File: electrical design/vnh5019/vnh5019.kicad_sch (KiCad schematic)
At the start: 20 parts, among them J1 XT30UPBF, J2 SH 1.0 6P, J3 Conn_01x01_Female, J4 Conn_01x01_Female, Q1 Q_NMOS_GDS, U1 VNH5019A-E

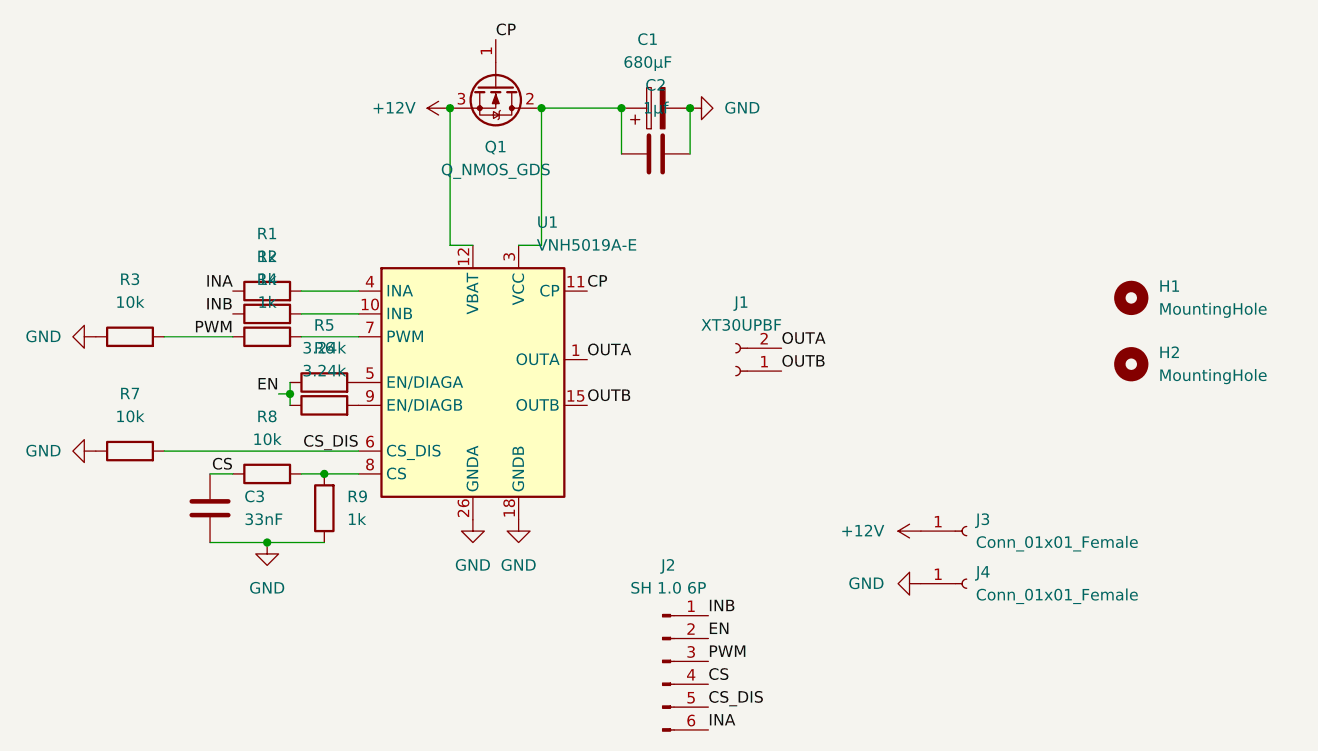
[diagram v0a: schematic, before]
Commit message: change driver output connector to 5 pins
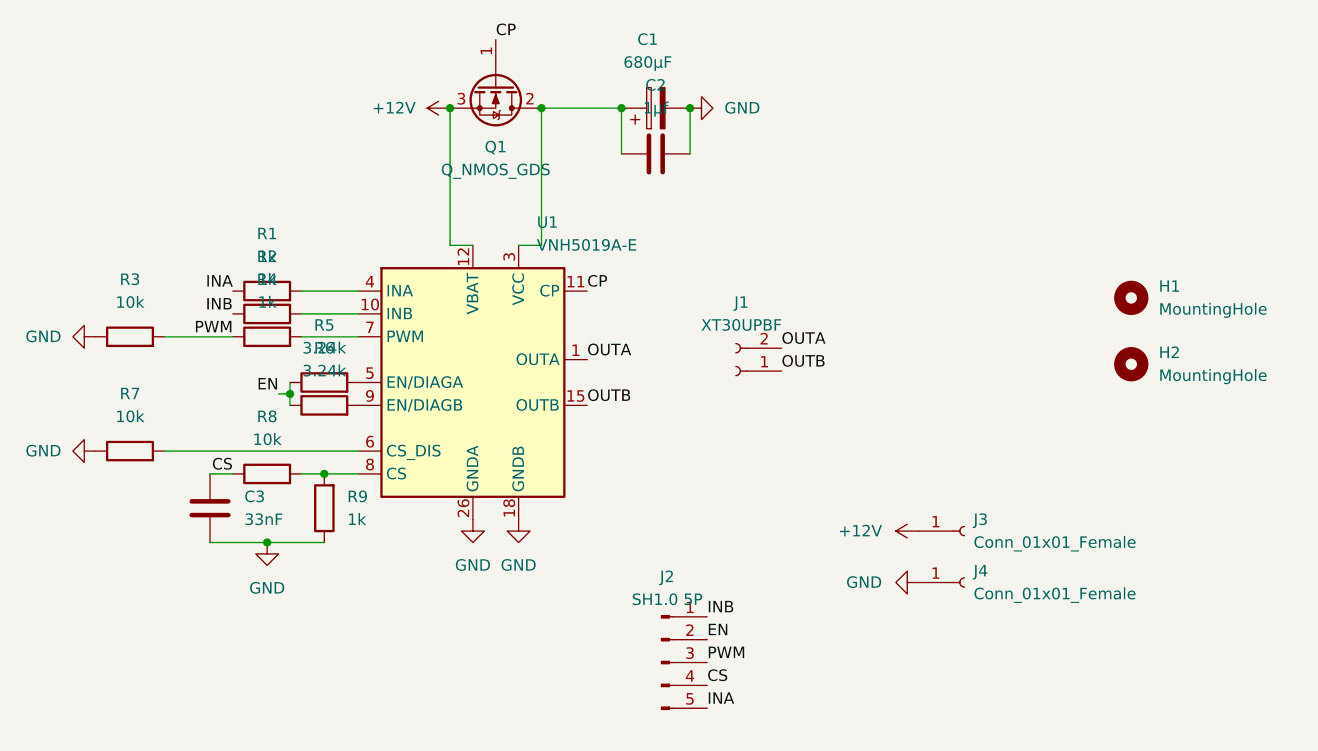
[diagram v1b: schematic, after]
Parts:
- removed J2: SH 1.0 6P, Connector_JST:JST_SH_SM06B-SRSS-TB_1x06-1MP_P1.00mm_Horizontal, symbol Connector:Conn_01x06_Male
- added J2: SH1.0 5P, Connector_JST:JST_SH_SM05B-SRSS-TB_1x05-1MP_P1.00mm_Horizontal, symbol Connector:Conn_01x05_Pin
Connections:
- net CS: now also J2.4 (Pin_4)
- net EN: now also J2.2 (Pin_2)
- net INA: now also J2.5 (Pin_5)
- net INB: now also J2.1 (Pin_1)
- net PWM: now also J2.3 (Pin_3)
- net CS_DIS: no longer names the net of R7.2, U1.6 (CS_DIS)

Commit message: add indicator leds to driver pcb
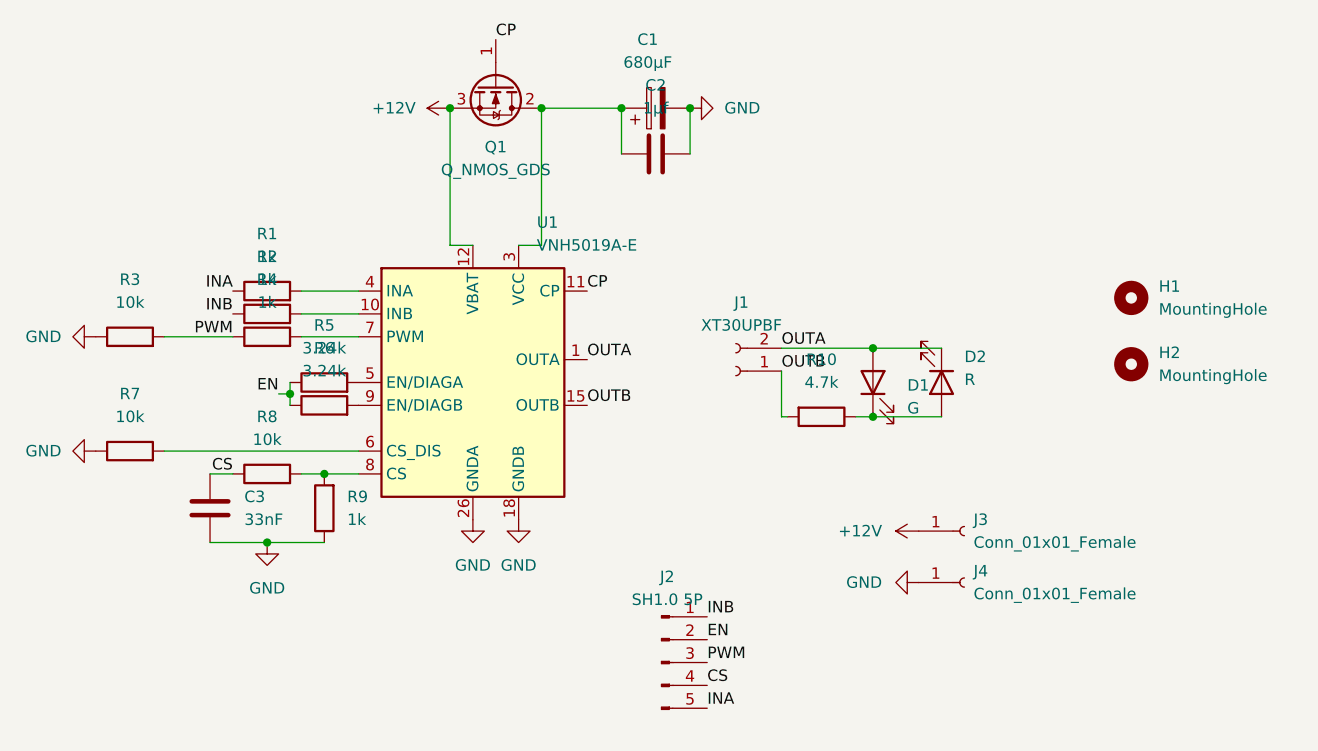
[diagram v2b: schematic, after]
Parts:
- added D1: G, Diode_SMD:D_0603_1608Metric, symbol Device:LED
- added D2: R, Diode_SMD:D_0603_1608Metric, symbol Device:LED
- added R10: 4.7k, Resistor_SMD:R_0603_1608Metric, symbol Device:R
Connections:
- net OUTA: now also D1.2 (A), D2.1 (K)
- net OUTB: now also R10.2
- new net: D1.1 (K), D2.2 (A), R10.1
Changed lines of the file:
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@@
   (junction (at 62.23 74.93) (diameter 0) (color 0 0 0 0)
   )
+  (junction (at 123.19 68.58) (diameter 0) (color 0 0 0 0)
+  )
   (junction (at 102.87 34.29) (diameter 0) (color 0 0 0 0)
   )
+  (junction (at 123.19 60.96) (diameter 0) (color 0 0 0 0)
+  )
   (junction (at 76.2 34.29) (diameter 0) (color 0 0 0 0)
   )
@@
     (stroke (width 0) (type default))
   )
+  (wire (pts (xy 123.19 68.58) (xy 130.81 68.58))
+    (stroke (width 0) (type default))
+  )
   (wire (pts (xy 59.69 59.69) (xy 66.04 59.69))
     (stroke (width 0) (type default))
@@
     (stroke (width 0) (type default))
   )
+  (wire (pts (xy 121.285 68.58) (xy 123.19 68.58))
+    (stroke (width 0) (type default))
+  )
   (wire (pts (xy 59.69 74.93) (xy 62.23 74.93))
     (stroke (width 0) (type default))
@@
     (stroke (width 0) (type default))
   )
+  (wire (pts (xy 113.03 63.5) (xy 113.03 68.58))
+    (stroke (width 0) (type default))
+  )
   (wire (pts (xy 95.25 34.29) (xy 95.25 39.37))
     (stroke (width 0) (type default))
   )
+  (wire (pts (xy 113.03 68.58) (xy 113.665 68.58))
+    (stroke (width 0) (type default))
+  )
   (wire (pts (xy 59.69 57.15) (xy 66.04 57.15))
     (stroke (width 0) (type default))
@@
     (stroke (width 0) (type default))
   )
+  (wire (pts (xy 123.19 60.96) (xy 130.81 60.96))
+    (stroke (width 0) (type default))
+  )
   (wire (pts (xy 86.36 49.53) (xy 86.36 34.29))
     (stroke (width 0) (type default))
   )
   (wire (pts (xy 83.82 49.53) (xy 86.36 49.53))
+    (stroke (width 0) (type default))
+  )
+  (wire (pts (xy 113.03 60.96) (xy 123.19 60.96))
     (stroke (width 0) (type default))
   )
@@
     )
   )
+  (symbol (lib_id "Device:R") (at 117.475 68.58 270) (unit 1)
+    (in_bom yes) (on_board yes) (dnp no) (fields_autoplaced)
+    (property "Reference" "R10" (at 117.475 62.23 90)
+      (effects (font (size 1.27 1.27)))
+    )
+    (property "Value" "4.7k" (at 117.475 64.77 90)
+      (effects (font (size 1.27 1.27)))
+    )
+    (property "Footprint" "Resistor_SMD:R_0603_1608Metric" (at 117.475 66.802 90)
+      (effects (font (size 1.27 1.27)) hide)
+    )
+    (property "Datasheet" "~" (at 117.475 68.58 0)
+      (effects (font (size 1.27 1.27)) hide)
+    )
+    (pin "2")
+    (pin "1")
+    (instances
+      (project "vnh5019"
+        (path "/7e5ca1ba-efa1-4ab9-9021-878f3c428475"
+          (reference "R10") (unit 1)
+        )
+      )
+    )
+  )
   (symbol (lib_id "Device:R") (at 55.88 54.61 90) (unit 1)
     (in_bom yes) (on_board yes) (dnp no) (fields_autoplaced)
@@
         (path "/7e5ca1ba-efa1-4ab9-9021-878f3c428475"
           (reference "#PWR05") (unit 1)
+        )
+      )
+    )
+  )
+  (symbol (lib_id "Device:LED") (at 130.81 64.77 270) (unit 1)
+    (in_bom yes) (on_board yes) (dnp no) (fields_autoplaced)
+    (property "Reference" "D2" (at 133.35 61.9125 90)
+      (effects (font (size 1.27 1.27)) (justify left))
+    )
+    (property "Value" "R" (at 133.35 64.4525 90)
+      (effects (font (size 1.27 1.27)) (justify left))
+    )
+    (property "Footprint" "Diode_SMD:D_0603_1608Metric" (at 130.81 64.77 0)
+      (effects (font (size 1.27 1.27)) hide)
+    )
+    (property "Datasheet" "~" (at 130.81 64.77 0)
+      (effects (font (size 1.27 1.27)) hide)
+    )
+    (pin "1")
+    (pin "2")
+    (instances
+      (project "vnh5019"
+        (path "/7e5ca1ba-efa1-4ab9-9021-878f3c428475"
+          (reference "D2") (unit 1)
         )
       )
@@
         )
       )
+    )
+  )
+  (symbol (lib_id "Device:LED") (at 123.19 64.77 90) (unit 1)
+    (in_bom yes) (on_board yes) (dnp no) (fields_autoplaced)
+    (property "Reference" "D1" (at 127 65.0875 90)
+      (effects (font (size 1.27 1.27)) (justify right))
+    )
+    (property "Value" "G" (at 127 67.6275 90)
+      (effects (font (size 1.27 1.27)) (justify right))
+    )
+    (property "Footprint" "Diode_SMD:D_0603_1608Metric" (at 123.19 64.77 0)
+      (effects (font (size 1.27 1.27)) hide)
+    )
+    (property "Datasheet" "~" (at 123.19 64.77 0)
+      (effects (font (size 1.27 1.27)) hide)
+    )
+    (pin "1")
+    (pin "2")
+    (instances
+      (project "vnh5019"
+        (path "/7e5ca1ba-efa1-4ab9-9021-878f3c428475"
+          (reference "D1") (unit 1)
+        )
+      )
